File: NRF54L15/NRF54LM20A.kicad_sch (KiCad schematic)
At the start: 39 parts, among them J1 Conn_ARM_SWD_TagConnect_TC203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, U1 S25HS512TFANHI010, U2 nRF54LM20A-QGAA, Y1 CX2016DB32000D0WZRC1

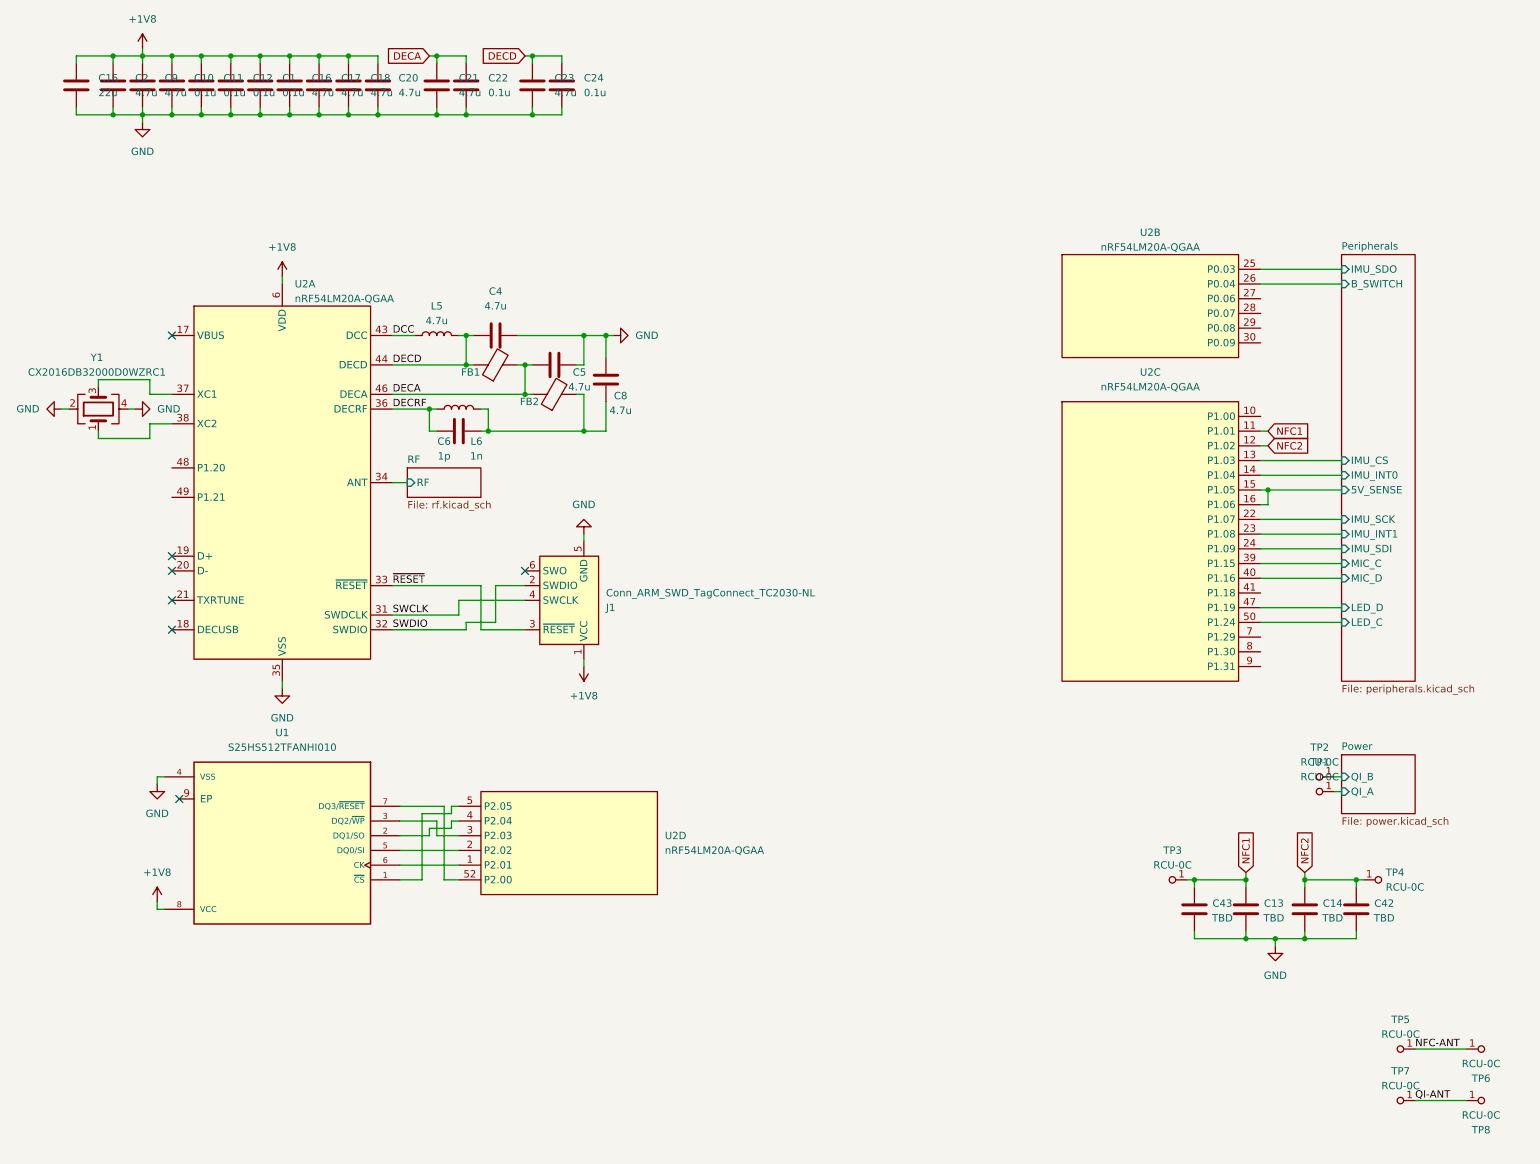
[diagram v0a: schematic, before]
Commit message: switch to nrf54l15, antenna work
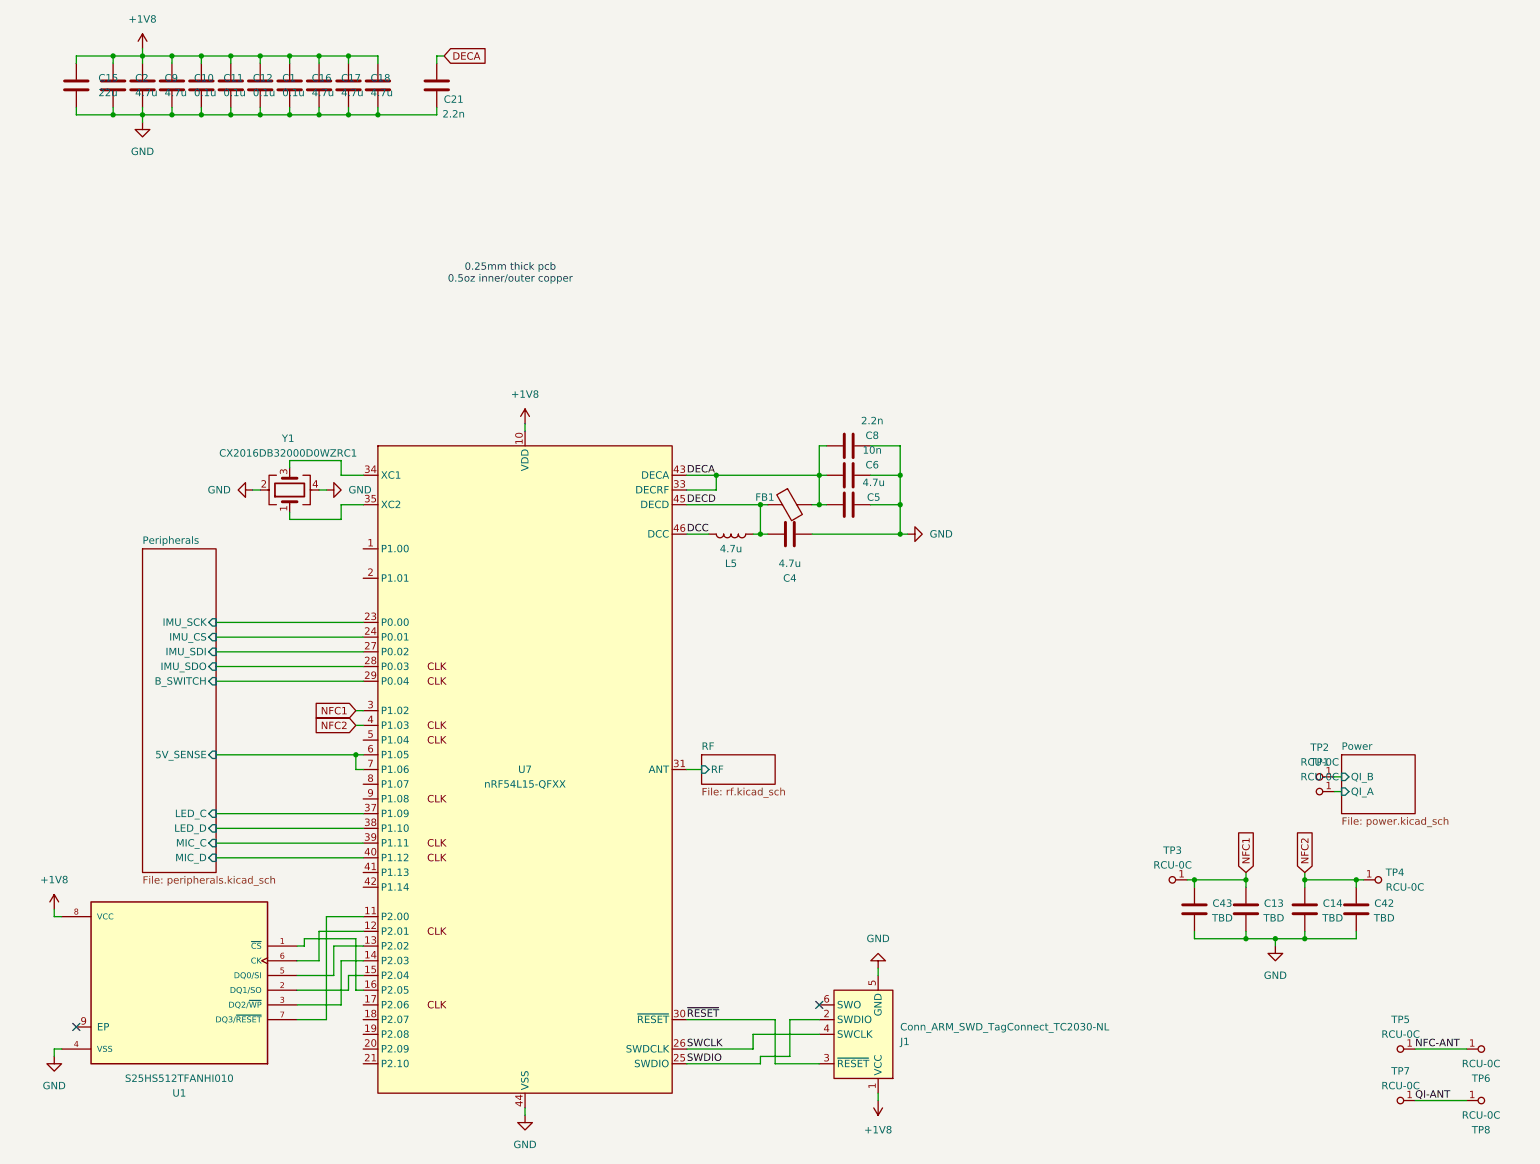
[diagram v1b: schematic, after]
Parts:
- removed C22, C24: 0.1u, Capacitor_SMD:C_0201_0603Metric, symbol Device:C
- removed C23: 4.7u, Capacitor_SMD:C_0201_0603Metric, symbol Device:C
- removed FB2: FerriteBead, Inductor_SMD:L_0201_0603Metric, symbol Device:FerriteBead
- removed L6: 1n, Inductor_SMD:L_0201_0603Metric, symbol Device:L
- removed U2: nRF54LM20A-QGAA, nordic-lib-kicad-nrf54l:QFN-52-1EP_6x6mm_P0.4mm_EP4.7x4.7mm_ThermalVias, symbol nordic-lib-kicad-nrf54l:nRF54LM20A-QGAA
- added U7: nRF54L15-QFXX, Package_DFN_QFN:QFN-48-1EP_6x6mm_P0.4mm_EP4.6x4.6mm, symbol nordic-lib-kicad-nrf54l:nRF54L15-QFXX
- C21, C8: value 4.7u -> 2.2n
- C6: value 1p -> 10n
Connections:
- net DECRF is gone; now on net GND: C6.1
- net +1V8: now also U7.10 (VDD), U7.22 (VDD), U7.36 (VDD), U7.47 (VDD), U7.48 (VDD)
- net DCC: now also U7.46 (DCC)
- net DECA: now also C6.2, C8.2, U7.33 (DECRF), U7.43 (DECA)
- net DECD: now also U7.45 (DECD)
- net GND: now also C8.1, U7.32 (VSS_PA), U7.44 (VSS), U7.49 (VSS); no longer C8.2
- net NFC1: now also U7.3 (P1.02)
- net NFC2: now also U7.4 (P1.03)
- net Peripherals/5V_SENSE: now also U7.6 (P1.05), U7.7 (P1.06)
- net Peripherals/B_SWITCH: now also U7.29 (P0.04)
- net Peripherals/IMU_CS: now also U7.24 (P0.01)
- net Peripherals/IMU_SCK: now also U7.23 (P0.00)
- net Peripherals/IMU_SDI: now also U7.27 (P0.02)
- net Peripherals/IMU_SDO: now also U7.28 (P0.03)
- net Peripherals/LED_C: now also U7.37 (P1.09)
- net Peripherals/LED_D: now also U7.38 (P1.10)
- net Peripherals/MIC_C: now also U7.39 (P1.11)
- net Peripherals/MIC_D: now also U7.40 (P1.12)
- net RF/RF: now also U7.31 (ANT)
- net SWCLK: now also U7.26 (SWDCLK)
- net SWDIO: now also U7.25 (SWDIO)
- net ~{RESET}: now also U7.30 (~{RESET})
- net at U1.6 (CK): now also U7.12 (P2.01)
- net at U1.5 (DQ0/SI): now also U7.13 (P2.02)
- net at U1.3 (DQ2/~{WP}): now also U7.14 (P2.03)
- net at U1.2 (DQ1/SO): now also U7.15 (P2.04)
- net at U1.1 (~{CS}): now also U7.16 (P2.05)
- net at U1.7 (DQ3/~{RESET}): now also U7.11 (P2.00)
- net at Y1.3: now also U7.34 (XC1)
- net at Y1.1: now also U7.35 (XC2)
- no-connect marks 7 -> 2
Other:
- sheet Peripherals ports: added none; removed IMU_INT0, IMU_INT1
- note added: "0.25mm thick pcb 0.5oz inner/outer copper"
- moved on the sheet: C4, C5, FB1, J1, L5, U1, Y1

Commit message: nfc rect
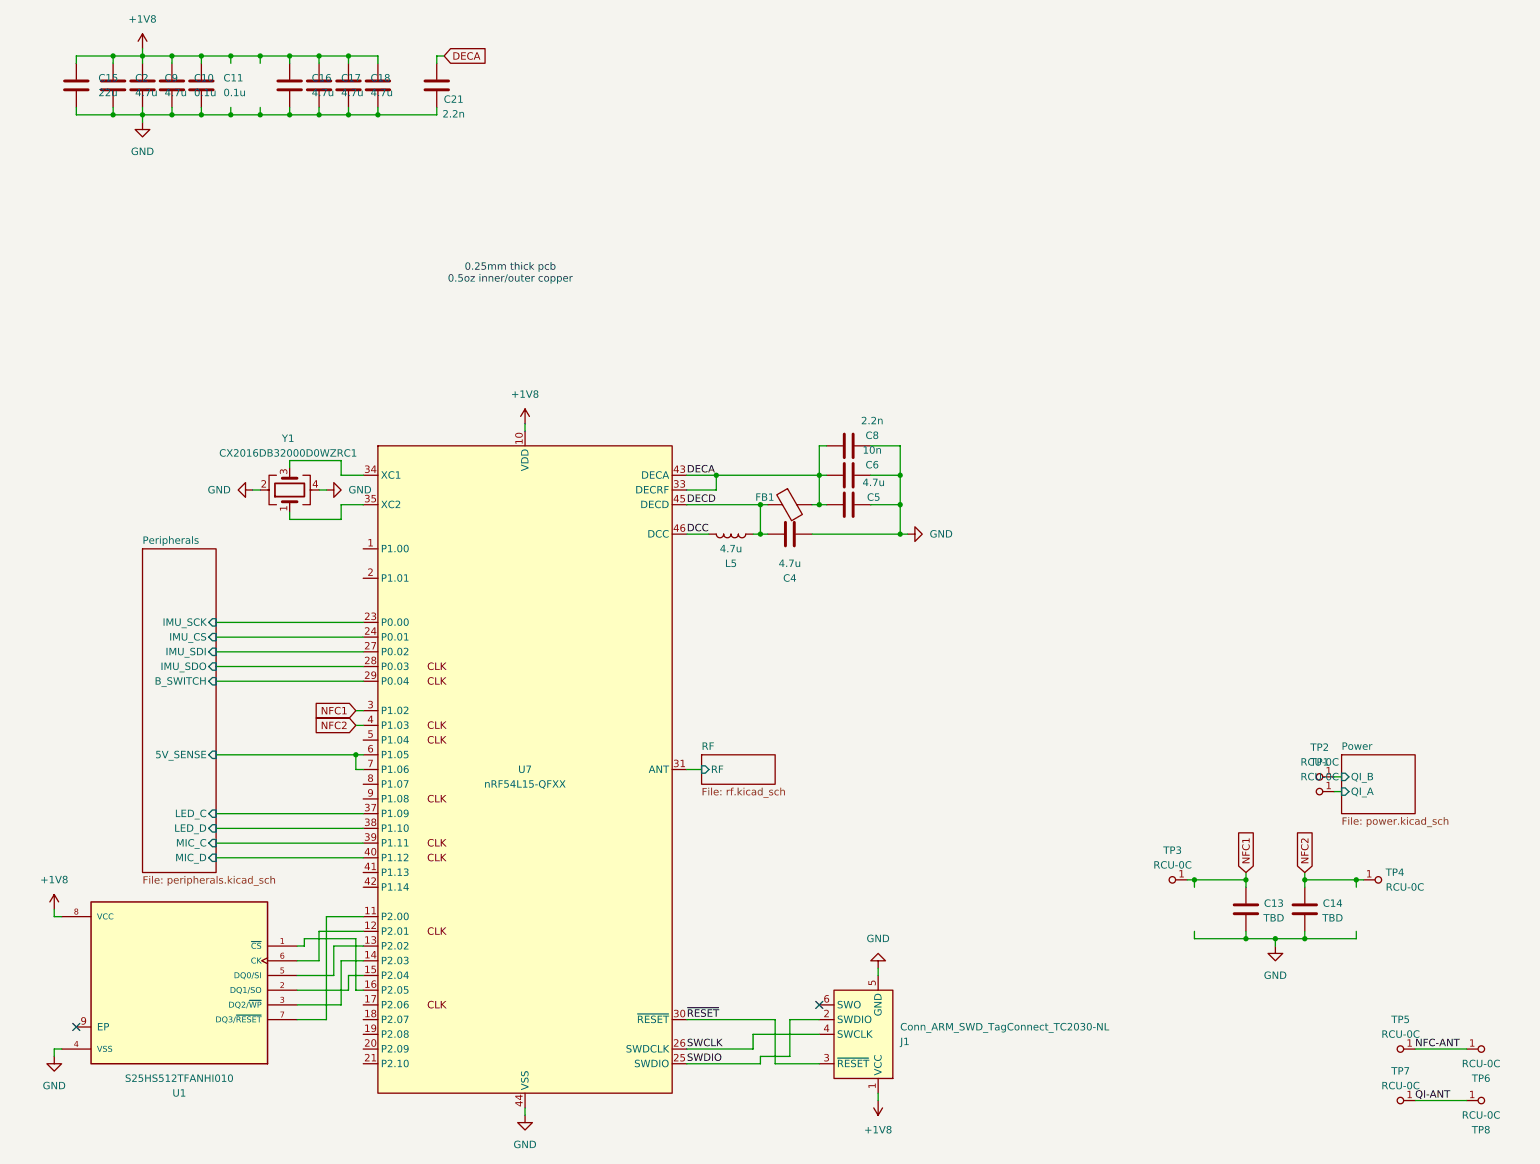
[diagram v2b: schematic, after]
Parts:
- removed C1, C12: 0.1u, Capacitor_SMD:C_0201_0603Metric, symbol Device:C
- removed C42, C43: TBD, Capacitor_SMD:C_0201_0603Metric, symbol Device:C
